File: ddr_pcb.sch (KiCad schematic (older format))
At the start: 17 parts, among them J1 Screw_Terminal_01x04, J2 Screw_Terminal_01x04, J3 Screw_Terminal_01x04, J4 Screw_Terminal_01x06, J5 Screw_Terminal_01x04, U1 ProMicro

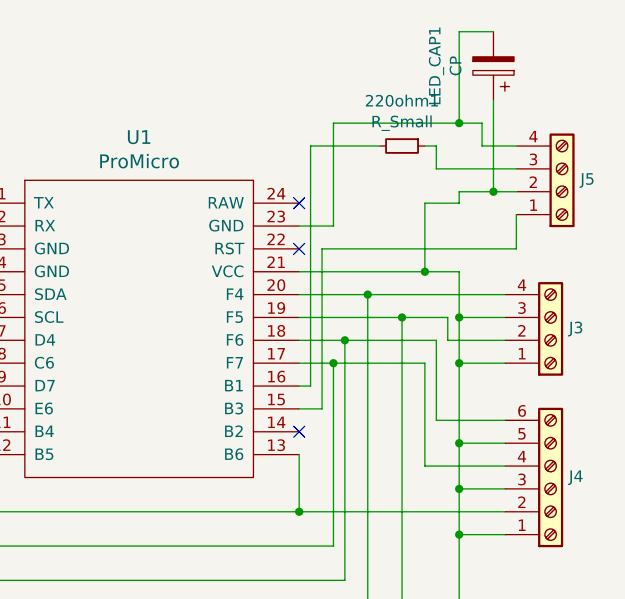
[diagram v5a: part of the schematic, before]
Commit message: new: Update pins to use 15/16 for SPI. Swap Pin1 to dat for non-SPI LEDs
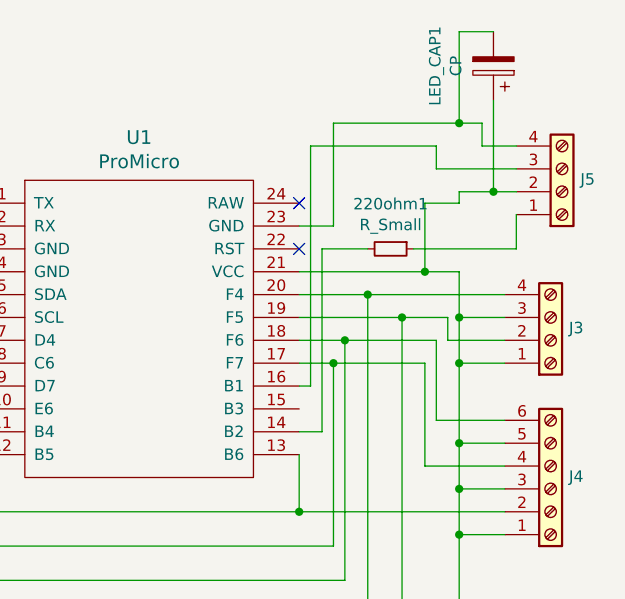
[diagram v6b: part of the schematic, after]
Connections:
- net at U1.14 (B2): now also 220ohm1.2
- net at U1.15 (B3): no longer J5.1 (Pin_1)
- net at U1.16 (B1): now also J5.3 (Pin_3); no longer 220ohm1.2
- net at 220ohm1.1: now also J5.1 (Pin_1); no longer J5.3 (Pin_3)
- no-connect marks 10 -> 9
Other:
- moved on the sheet: 220ohm1
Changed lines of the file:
@@
 	4450 3550 4650 3550
-Wire Wire Line
-	4000 3650 4200 3650
-Wire Wire Line
-	4200 3650 4200 4700
 Wire Wire Line
 	4000 4150 4000 4400
@@
 	4000 3550 4450 3550
 Wire Wire Line
-	4200 3650 4600 3650
-Wire Wire Line
 	4600 3650 4600 4000
 Wire Wire Line
 	4600 4000 4900 4000
-Connection ~ 4200 3650
 Wire Wire Line
 	4550 3750 4550 4200
@@
 	4150 3150 4000 3150
 Wire Wire Line
-	4000 3850 4050 3850
-Wire Wire Line
-	4050 3850 4050 2800
-Wire Wire Line
-	4050 2800 4350 2800
-Wire Wire Line
 	4150 2700 4150 3150
 $Comp
 L Device:R_Small 220ohm1
 U 1 1 61A07599
-P 4450 2800
-F 0 "220ohm1" V 4254 2800 50  0000 C CNN
-F 1 "R_Small" V 4345 2800 50  0000 C CNN
-F 2 "ddr_pcb:R_Axial_DDRPAD_L3.6mm_D1.6mm_P7.62mm_Horizontal" H 4450 2800 50  0001 C CNN
-F 3 "~" H 4450 2800 50  0001 C CNN
-	1    4450 2800
+P 4400 3250
+F 0 "220ohm1" V 4204 3250 50  0000 C CNN
+F 1 "R_Small" V 4295 3250 50  0000 C CNN
+F 2 "ddr_pcb:R_Axial_DDRPAD_L3.6mm_D1.6mm_P7.62mm_Horizontal" H 4400 3250 50  0001 C CNN
+F 3 "~" H 4400 3250 50  0001 C CNN
+	1    4400 3250
 	0    1    1    0
 $EndComp
@@
 Wire Wire Line
 	4550 3050 4700 3050
-Wire Wire Line
-	4550 2800 4600 2800
 Wire Wire Line
 	4600 2800 4600 2900
@@
 NoConn ~ 4000 3050
 NoConn ~ 4000 3250
-NoConn ~ 4000 4050
 Wire Wire Line
 	4000 3750 4150 3750
@@
 	2250 4550 4150 4550
 Wire Wire Line
-	4000 3950 4100 3950
-Wire Wire Line
-	4100 3950 4100 3250
-Wire Wire Line
-	4100 3250 4950 3250
+	4100 3250 4300 3250
 Wire Wire Line
 	4950 3250 4950 3100
+Wire Wire Line
+	4200 3650 4600 3650
+Wire Wire Line
+	4000 3650 4200 3650
+Connection ~ 4200 3650
+Wire Wire Line
+	4200 3650 4200 4700
+Wire Wire Line
+	4000 4050 4100 4050
+Wire Wire Line
+	4100 4050 4100 3250
+Wire Wire Line
+	4050 2800 4050 3850
+Wire Wire Line
+	4050 3850 4000 3850
+Wire Wire Line
+	4500 3250 4950 3250
+Wire Wire Line
+	4050 2800 4600 2800
 $EndSCHEMATC
